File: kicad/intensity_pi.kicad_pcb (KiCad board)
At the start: 4 copper layers, 144.8 x 171.5 mm, 131 parts, among them J1 Input A, J2 Input B / Setpoint, J3 Monitor, J4 Output, J5 Screw_Terminal_01x02, J7 select 1, Q1 2N7002E, Q2 2N7002E, SW1 SW_SPDT, SW2 SW_SPDT, SW3 SW_SPDT, U1 LM4040DBZ-5, U10 OPA189, U11 PC817, U12 OPA189, U13 BUF634A, U14 TMUX6123, U17 TMUX6123, U18 OPA189, U19 L7815, U2 LM4040DBZ-5, U20 OPA189, U21 OPA189, U23 L7915, U3 INA849, U4 INA849, U5 OPA189, U6 LM2937-5, U7 OPA189, U8 BUF634A, U9 LM317_TO-252

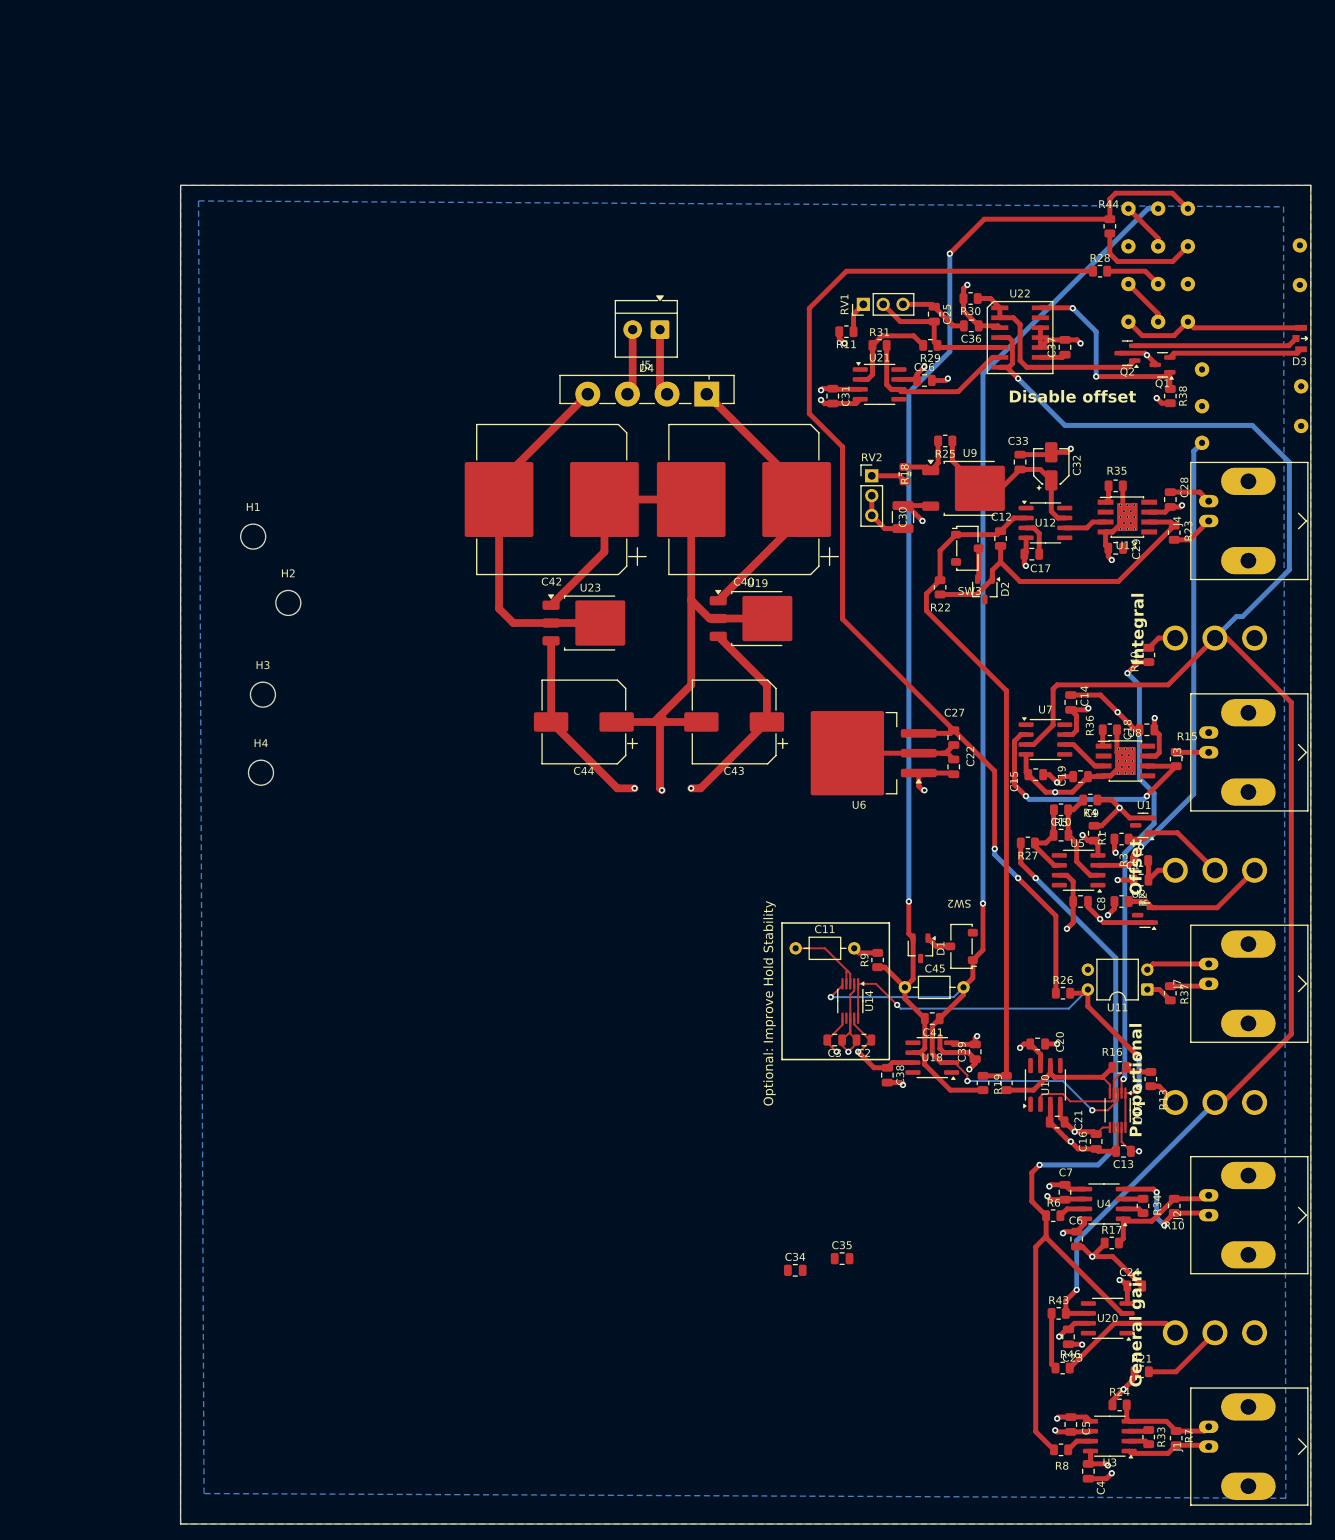
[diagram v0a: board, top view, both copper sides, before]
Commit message: Fixed LED Threshold schematic, added second power input screw terminal, first attempt at final placement and routing
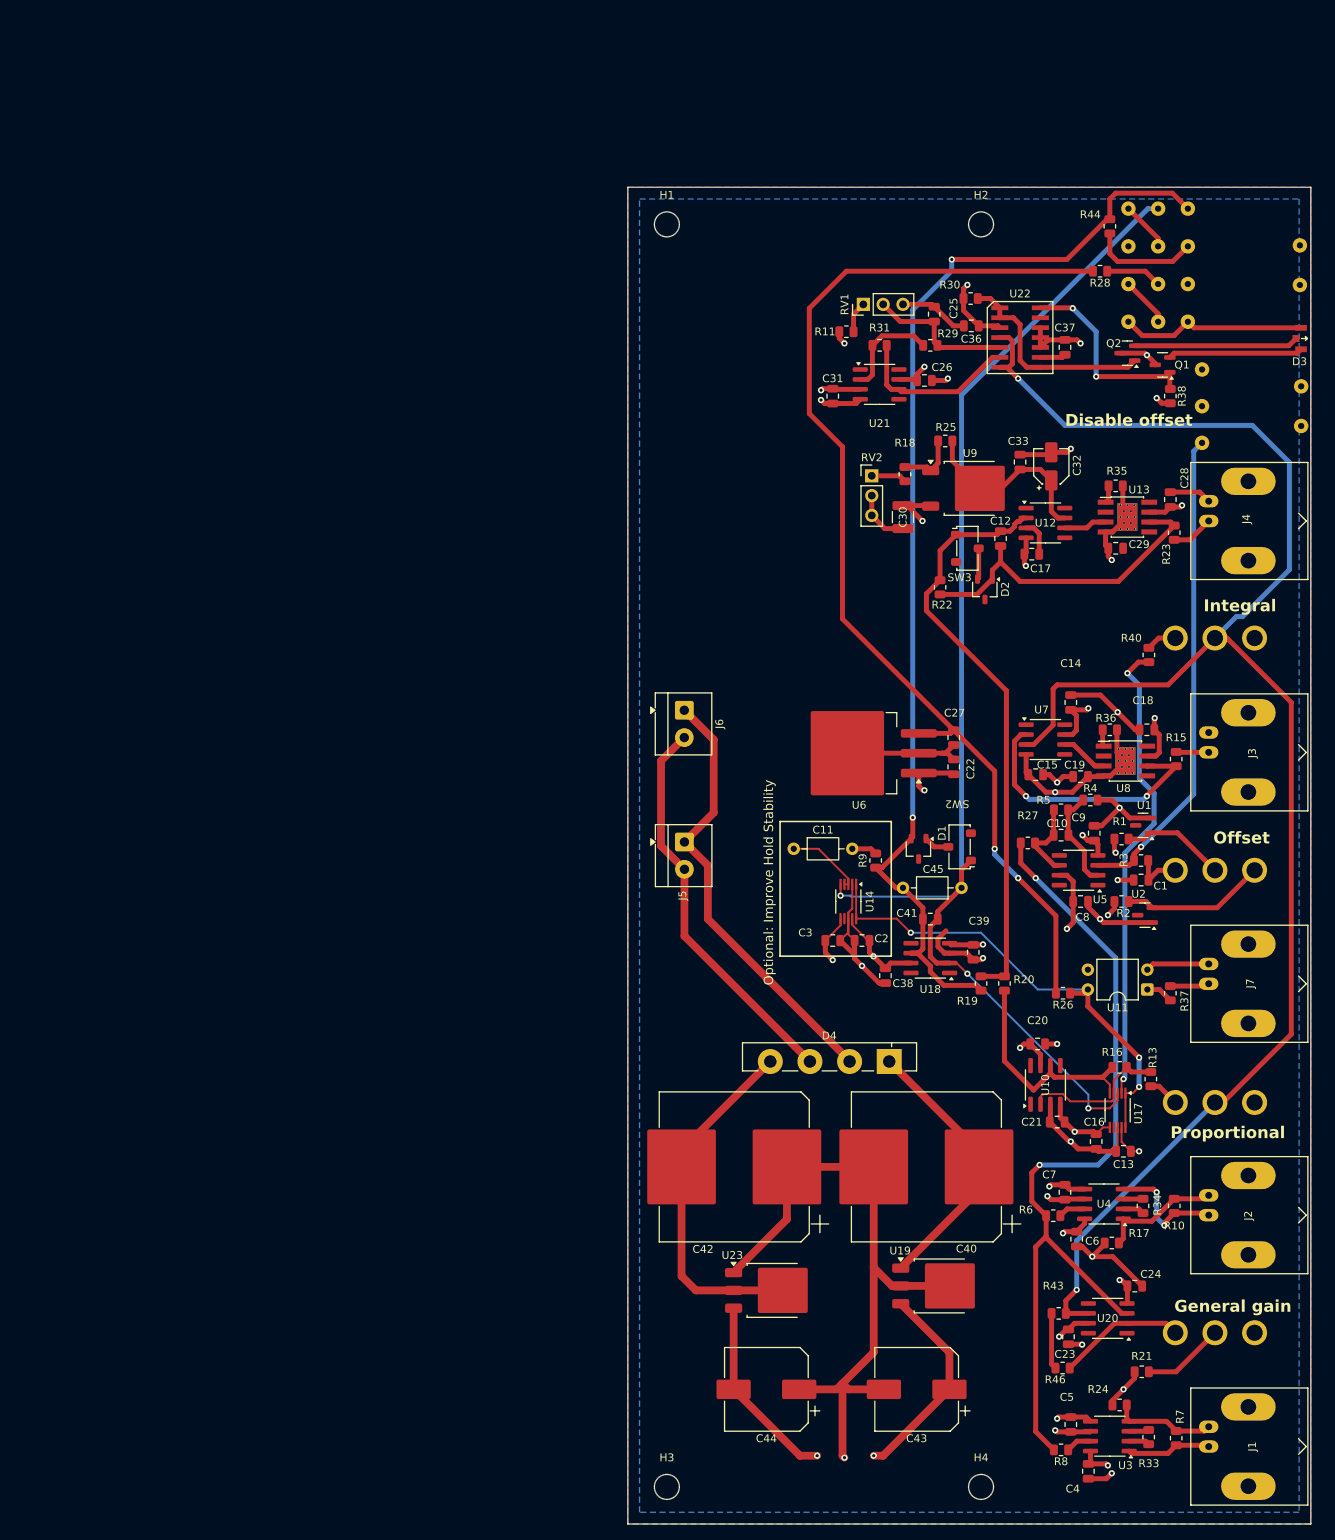
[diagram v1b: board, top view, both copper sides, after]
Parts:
- removed C34, C35: 100nF, Capacitor_SMD:C_0805_2012Metric
- added J6: Screw_Terminal_01x02, TerminalBlock_4Ucon:TerminalBlock_4Ucon_1x02_P3.50mm_Horizontal, F.Cu at (178.2, 48.8)
- SW5: value ~ -> EG6100-ND
- U22: value ~ -> 4x Comparator
- moved H4 129.9 mm to (216.2, 148.2)
- moved H3 113.9 mm to (176.0, 148.2)
- moved H2 101.1 mm to (216.2, -13.5)
- moved C40 88.6 mm to (209.2, 107.2)
- moved C42 88.6 mm to (184.6, 107.2)
- moved C43 88.6 mm to (208.0, 135.8)
- moved C44 88.6 mm to (188.8, 135.8)
- moved D4 88.6 mm to (204.5, 93.8)
- moved U19 88.6 mm to (211.0, 122.5)
- moved U23 88.6 mm to (189.6, 123.1)
- moved H1 66.4 mm to (176.0, -13.5)
- moved J5 65.7 mm to (178.2, 65.6), turned to -90 degrees
- moved C11 12.8 mm to (192.2, 66.5)
- moved C2 12.8 mm to (201.0, 78.2)
- moved C3 12.8 mm to (197.2, 78.2)
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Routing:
- net -15V RMS AC: track 8.64 -> 56.8 mm
- net +15V RMS AC: track 7.60 -> 50.6 mm
- net Net-(D1-A): track 158.6 -> 144.8 mm
- net Net-(SW3-A): track 88.0 -> 75.5 mm
- net Net-(R16-Pad2): track 18.6 -> 29.4 mm
- net GND: track 266.0 -> 271.8 mm, vias 21 -> 20
- net Net-(SW2-A): track 168.9 -> 164.6 mm, vias 4 -> 3
- net +15V: track 122.0 -> 119.4 mm
- net Net-(U14C-SEL1): track 60.3 -> 62.0 mm
- net Net-(C11-Pad1): track 11.4 -> 9.81 mm
- net -15V: track 113.0 -> 114.3 mm
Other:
- board size 144.8 x 171.5 mm -> 87.5 x 171.2 mm

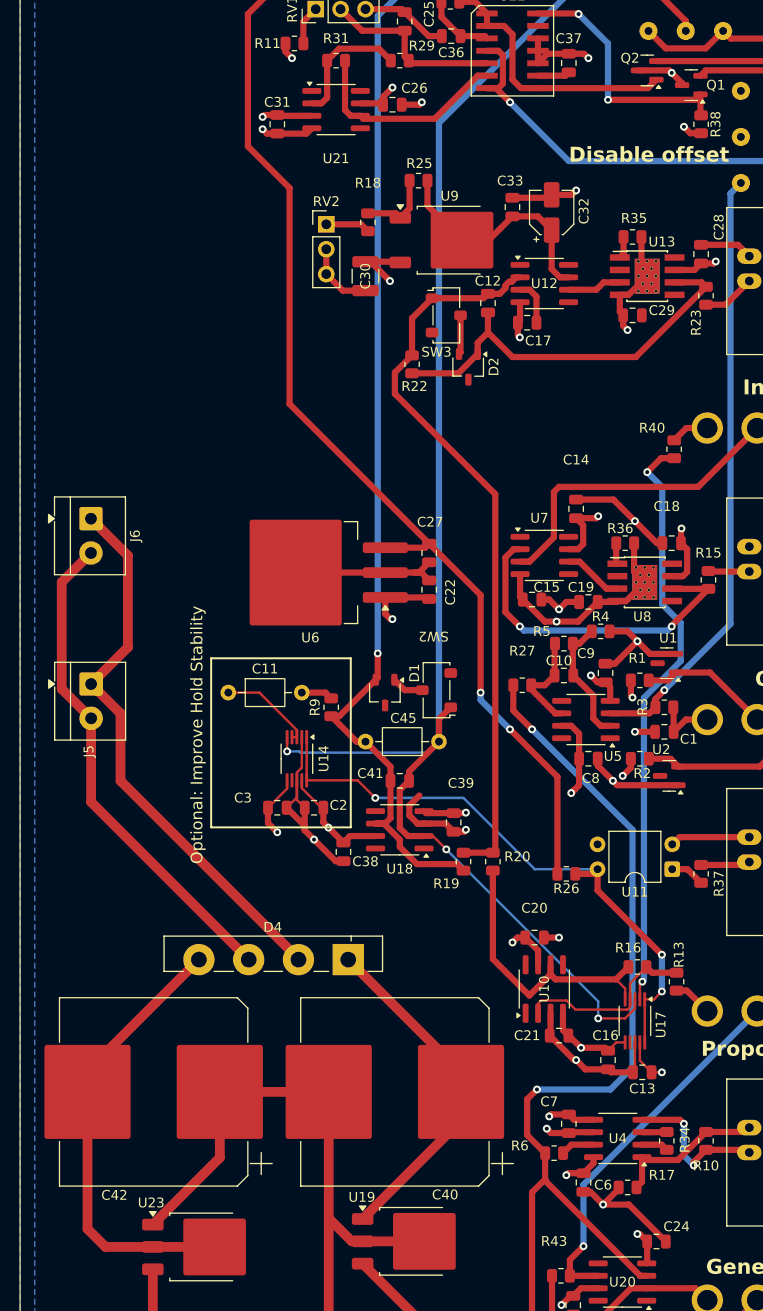
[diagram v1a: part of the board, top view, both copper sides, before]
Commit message: Removed large cap and rectifier, added transistor resistors
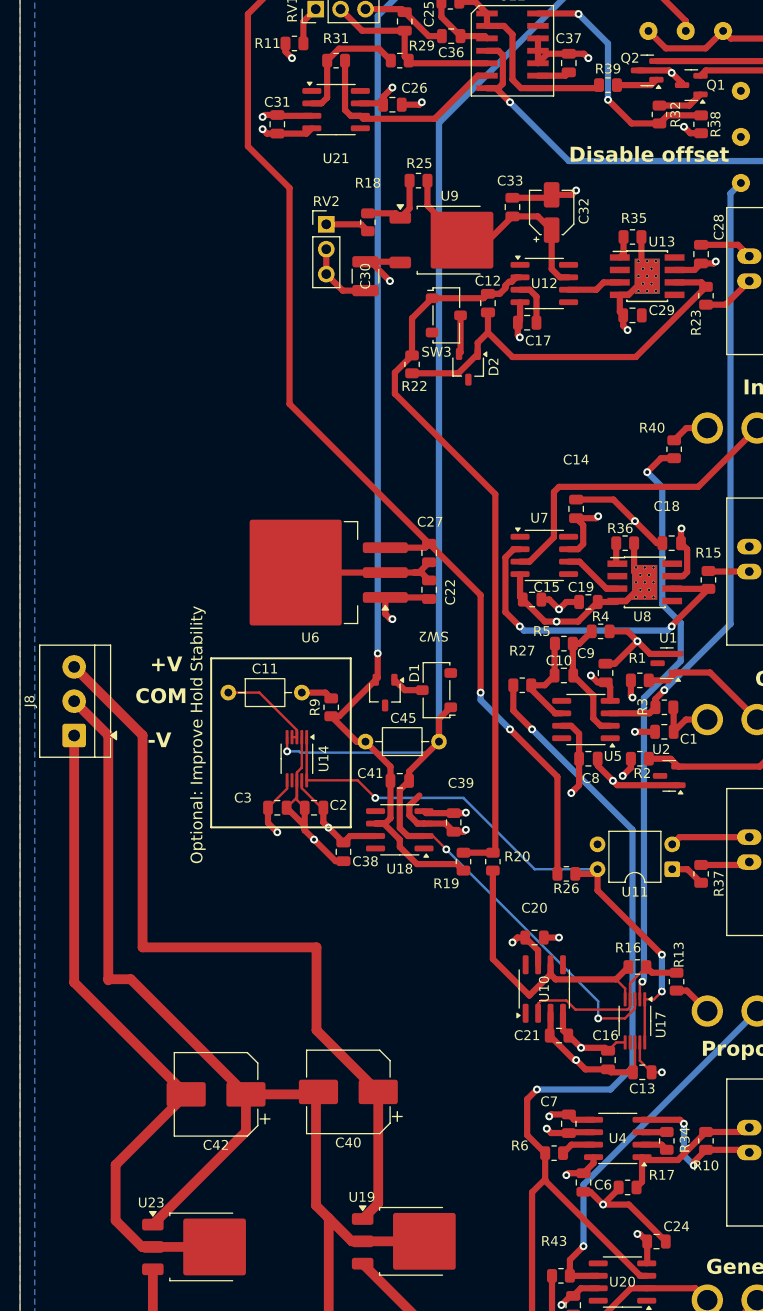
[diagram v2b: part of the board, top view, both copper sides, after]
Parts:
- removed D4: GBU4A, Diode_THT:Diode_Bridge_Vishay_GBU
- removed J5, J6: Screw_Terminal_01x02, TerminalBlock_4Ucon:TerminalBlock_4Ucon_1x02_P3.50mm_Horizontal
- added J8: Screw_Terminal_01x03, TerminalBlock_4Ucon:TerminalBlock_4Ucon_1x03_P3.50mm_Horizontal, F.Cu at (176.5, 70.9)
- added R32: 100, Resistor_SMD:R_0805_2012Metric, F.Cu at (236.2, 7.50)
- added R39: 100, Resistor_SMD:R_0805_2012Metric, F.Cu at (231.0, 4.50)
- C40, C42: value 3000uF -> 100uF; footprint Capacitor_SMD:CP_Elec_18x22 -> Capacitor_SMD:CP_Elec_8x6.5
- moved C42 6.37 mm to (191.0, 107.5)
- moved C40 4.75 mm to (204.5, 107.2)
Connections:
- net GND renamed COMMON
- net Net-(D4-+) renamed +V_DC_unregulated
- net Net-(D4--) renamed -V_DC_unregulated
- R30 pad 1: Net-(Q2-G) -> Net-(U22C--)
- R38 pad 1: Net-(Q1-G) -> Net-(R32-Pad2)
- U22 pad 1: Net-(Q2-G) -> Net-(U22C--)
- U22 pad 14: Net-(Q1-G) -> Net-(R32-Pad2)
- U22 pad 2: Net-(Q2-G) -> Net-(U22C--)
- U22 pad 8: Net-(Q2-G) -> Net-(U22C--)
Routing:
- net -15V RMS AC: track 56.8 -> 0.00 mm
- net +15V RMS AC: track 50.6 -> 0.00 mm
- net +V_DC_unregulated: track 30.5 -> 80.3 mm
- net COMMON: track 271.8 -> 317.9 mm
- net Net-(R32-Pad2): track 0.00 -> 25.0 mm, vias 0 -> 2
- net -V_DC_unregulated: track 43.8 -> 68.4 mm
- net Net-(Q2-G): track 27.6 -> 4.25 mm
- net Net-(U22C--): track 0.00 -> 21.5 mm
- net Net-(Q1-G): track 25.9 -> 4.66 mm, vias 2 -> 0
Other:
- board text added: "+V"
- board text added: "-V"
- board text added: "COM"

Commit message: Final Schematic, Reworking PCB pt 1
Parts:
- C11: footprint Capacitor_THT:C_Axial_L3.8mm_D2.6mm_P7.50mm_Horizontal -> Capacitor_SMD:C_0805_2012Metric
- moved R13 183.2 mm to (94.0, -17.2), turned to 0 degrees
- moved U17 172.8 mm to (106.4, -16.8)
- moved C13 172.8 mm to (107.4, -11.8), turned to -90 degrees
- moved R16 172.5 mm to (102.5, -17.2), turned to 90 degrees
- moved C16 171.4 mm to (104.8, -11.9)
- moved C20 170.0 mm to (97.7, -22.8), turned to 90 degrees
- moved U10 169.8 mm to (98.7, -17.3)
- moved C21 168.8 mm to (100.9, -11.8), turned to 90 degrees
- moved C2 153.4 mm to (99.0, -36.3), turned to 90 degrees
- moved C3 149.6 mm to (101.0, -36.3), turned to -90 degrees
- moved C38 146.9 mm to (101.3, -22.3), turned to 180 degrees
- moved C39 146.7 mm to (111.7, -24.2)
- moved C45 146.7 mm to (112.9, -35.0)
- moved U18 145.9 mm to (106.9, -23.0)
- moved C41 145.0 mm to (107.0, -26.8)
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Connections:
- net COMMON renamed GND
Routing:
- net GND: track 317.9 -> 184.4 mm, vias 20 -> 35
- net +V_DC_unregulated: track 80.3 -> 23.9 mm
- net -V_DC_unregulated: track 68.4 -> 18.3 mm
- net Net-(U14C-SEL1): track 62.0 -> 41.2 mm, vias 3 -> 4
- net Net-(SW2-A): track 164.6 -> 182.3 mm, vias 3 -> 4
- net Net-(U10--): track 19.1 -> 33.4 mm
- net -15V: track 114.3 -> 104.3 mm, vias 14 -> 17
- net +15V: track 119.4 -> 128.6 mm, vias 18 -> 20
- net Net-(R16-Pad2): track 29.4 -> 37.1 mm
- net Net-(D1-K): track 3.29 -> 10.2 mm
- net Net-(D1-A): track 144.8 -> 151.7 mm
- net Net-(C11-Pad1): track 9.81 -> 3.30 mm
- net Net-(R40-Pad2): track 60.3 -> 63.5 mm
- net Net-(R37-Pad1): track 3.52 -> 2.60 mm
- net Net-(J7-In): track 4.62 -> 3.75 mm
- added copper zone on F.Cu, net +V_DC_unregulated
- added copper zone on F.Cu, net -V_DC_unregulated
